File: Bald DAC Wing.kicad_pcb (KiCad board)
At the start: 4 copper layers, 45.5 x 46.5 mm, 50 parts, among them J1 PWR, J2 DAC_A_Out, J3 DAC_B_Out, J5 Z_Out, J6 Feather, J7 Data Debug Low, J8 High, U1 AD5447, U2 AD8065ARTZ, U3 AD8065ARTZ, U4 74LVC574APWR, U5 74LVC574APWR, U6 74LVC1G04, U7 REF3425

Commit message: It's getting there
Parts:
- removed J8: High, Connector_PinHeader_2.54mm:PinHeader_2x06_P2.54mm_Vertical
- removed TP12, TP13: TestPoint_Harwin, My Libraries:Harwin-S1751-46-Test-Point
- added H2: MountingHole_M2.5_Screw, MountingHole:MountingHole_2.7mm_M2.5, F.Cu at (102.5, 71.0)
- added J10: Ctrl Debug, Connector_PinHeader_2.54mm:PinHeader_2x04_P2.54mm_Vertical, F.Cu at (113.5, 86.3)
- added J9: Data Debug High, Connector_PinHeader_2.54mm:PinHeader_2x04_P2.54mm_Vertical, F.Cu at (113.5, 74.2)
- J7: footprint Connector_PinHeader_2.54mm:PinHeader_2x06_P2.54mm_Vertical -> Connector_PinHeader_2.54mm:PinHeader_2x04_P2.54mm_Vertical
- moved R73 8.32 mm to (118.8, 92.0), turned to 90 degrees
- moved C5 6.79 mm to (125.6, 97.2), turned to -90 degrees
- moved D1 5.07 mm to (122.5, 70.5)
- moved R61 5.07 mm to (126.5, 70.5)
- moved J7 4.81 mm to (113.5, 98.5)
- moved C15 4.33 mm to (108.0, 87.8), turned to 0 degrees
- moved C1 3.88 mm to (127.0, 76.0)
- moved C6 3.88 mm to (121.0, 76.0)
- moved TP6 3.88 mm to (123.7, 72.5)
- moved U2 3.88 mm to (123.7, 76.0)
- moved C11 3.54 mm to (124.5, 111.5)
- moved C12 3.54 mm to (117.5, 111.5)
- moved TP11 3.54 mm to (127.0, 111.5)
- moved TP5 3.54 mm to (115.0, 111.5)
- moved U7 3.54 mm to (121.5, 111.5)
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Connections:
- J7 pad 1: /DB3 -> /DB5
- J7 pad 2: /DB1 -> /DB4
- J7 pad 3: /DB2 -> /DB3
- J7 pad 4: /DB0 -> /DB2
- J7 pad 5: GND -> /DB1
- J7 pad 6: GND -> /DB0
- J7 pad 7: /DB7 -> GND
- J7 pad 8: /DB5 -> GND
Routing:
- net /DAC_AB: track 0.00 -> 52.1 mm, vias 0 -> 3
- net /~{CS}: track 0.00 -> 41.6 mm, vias 0 -> 1
- net /LCLKL: track 0.00 -> 41.5 mm, vias 0 -> 2
- net /LOE: track 0.00 -> 27.6 mm
- net /DB11: track 0.00 -> 24.3 mm
- net /DB0: track 0.00 -> 22.6 mm
- net /DB10: track 0.00 -> 22.6 mm
- net /DB1: track 0.00 -> 20.9 mm
- net /DB9: track 0.00 -> 20.7 mm
- net /LCLKH: track 0.00 -> 20.6 mm, vias 0 -> 1
- net /DB2: track 0.00 -> 19.2 mm
- net /DB8: track 0.00 -> 19.0 mm
- net /DB3: track 0.00 -> 17.6 mm
- net /DB7: track 0.00 -> 17.1 mm
- net /DB4: track 0.00 -> 16.2 mm
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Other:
- board size 45.5 x 46.5 mm -> 42 x 46.5 mm
- board text removed: "Should make it so feather sits over... adjust holes to match"

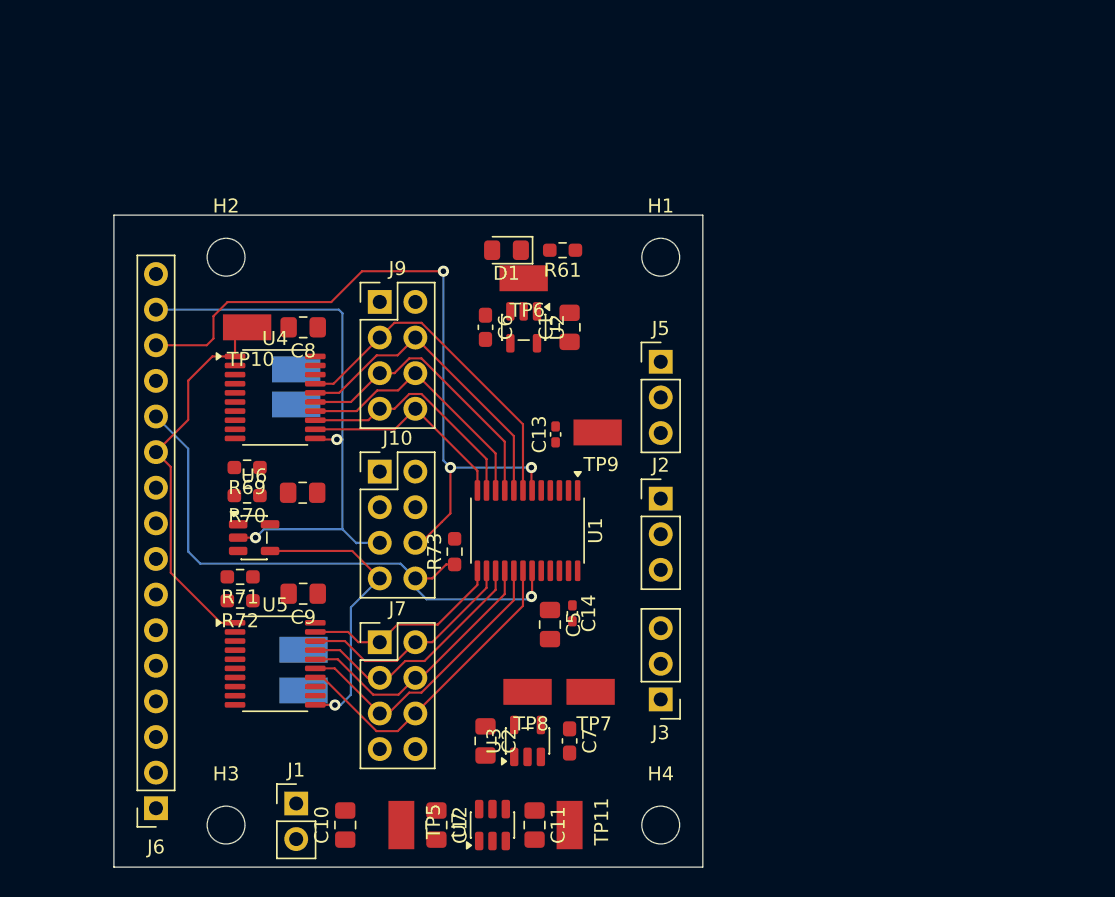
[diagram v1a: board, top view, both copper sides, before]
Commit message: added BNCs for ABZ
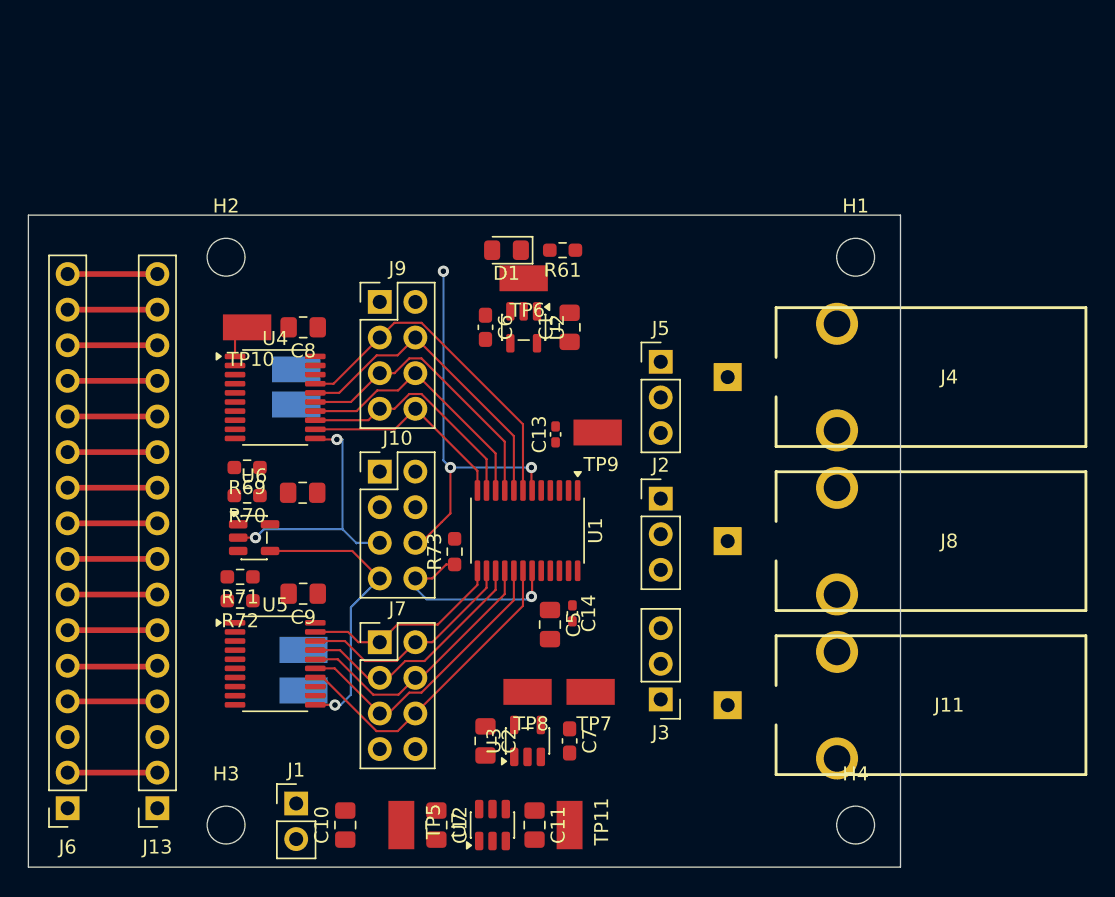
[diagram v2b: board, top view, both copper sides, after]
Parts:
- added J11: BNC_B, My Libraries:Molex_73100-0105_BNC_RA, F.Cu at (138.3, 103.0)
- added J13: Feather Debug, Connector_PinSocket_2.54mm:PinSocket_1x16_P2.54mm_Vertical, F.Cu at (97.6, 110.3)
- added J4: BNC_Z, My Libraries:Molex_73100-0105_BNC_RA, F.Cu at (138.3, 79.5)
- added J8: BNC_A, My Libraries:Molex_73100-0105_BNC_RA, F.Cu at (138.3, 91.2)
- moved H1 13.9 mm to (147.4, 71.0)
- moved H4 13.9 mm to (147.4, 111.5)
- moved J6 6.30 mm to (91.2, 110.3)
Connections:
- net Net-(J1-Pin_1) renamed /RawIn
- J5 pad 1: /Z_Blank -> unconnected-(J5-Pin_1-Pad1)
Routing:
- net /~{CS}: track 41.6 -> 20.5 mm
- net /LOE: track 27.6 -> 8.83 mm
- net /DAC_AB: track 52.1 -> 34.8 mm
- net /LCLKL: track 41.5 -> 25.5 mm
- net /D0: track 0.00 -> 6.45 mm
- net GND: track 0.00 -> 6.40 mm
- net /Z_Blank: track 0.00 -> 6.40 mm
- net /RawIn: track 0.00 -> 6.40 mm
- net /REF_EN: track 0.00 -> 6.40 mm
- net /D5: track 0.00 -> 6.40 mm
- net /D4: track 0.00 -> 6.40 mm
- net /D3: track 0.00 -> 6.40 mm
- net /D2: track 0.00 -> 6.40 mm
- net /D1: track 0.00 -> 6.40 mm
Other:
- board size 42 x 46.5 mm -> 62.2 x 46.5 mm

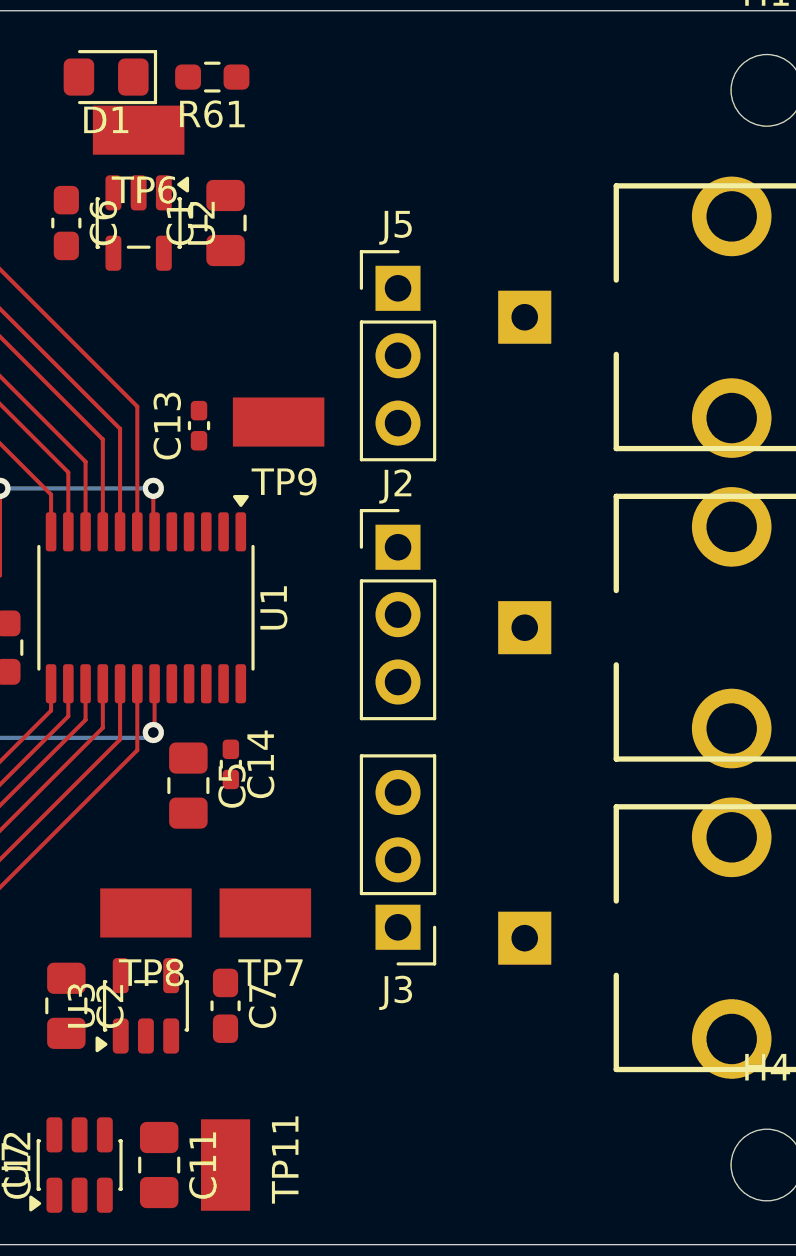
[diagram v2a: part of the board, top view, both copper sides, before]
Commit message: added JLC constraints (imported from clanker template)
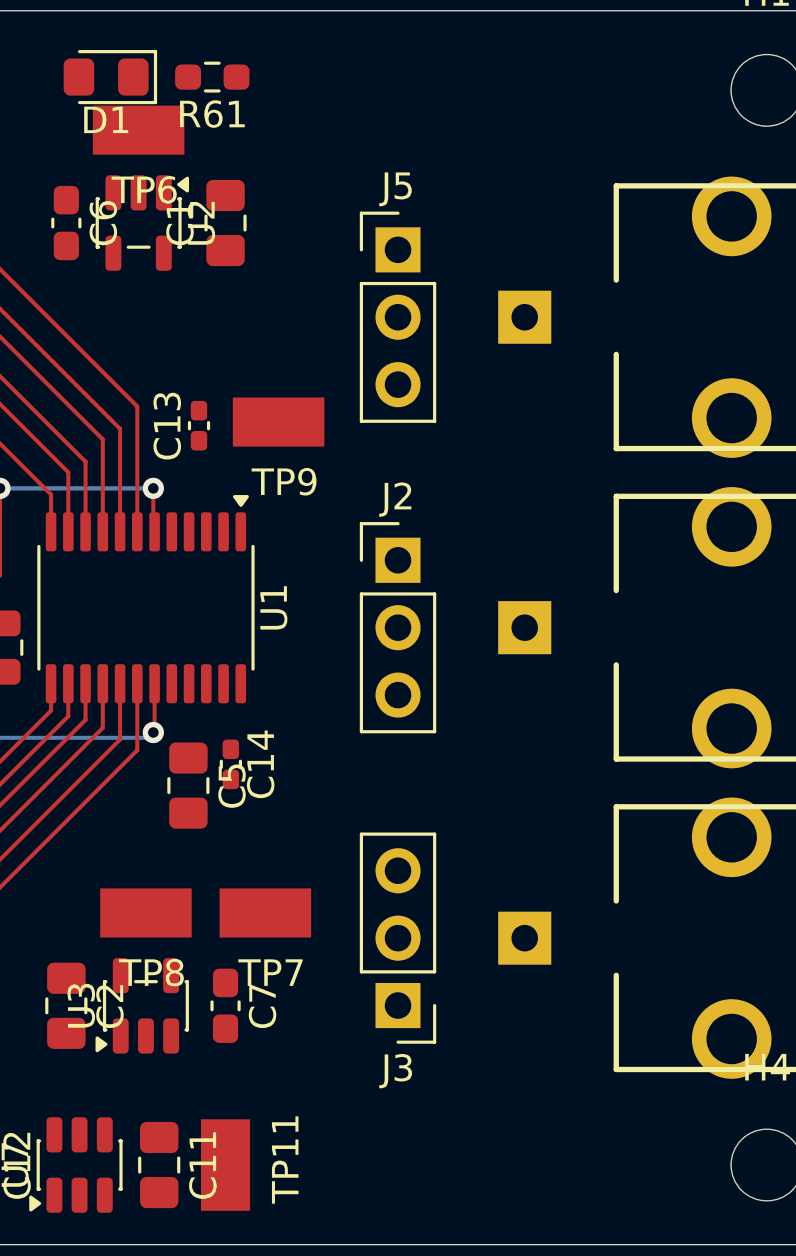
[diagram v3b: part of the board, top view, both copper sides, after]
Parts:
- moved J3 2.95 mm to (133.5, 105.5)
- moved J5 1.45 mm to (133.5, 77.0)
- moved J2 0.49 mm to (133.5, 88.7)
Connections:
- J2 pad 1: /OUT_A -> GND
- J2 pad 2: GND -> /OUT_A
- J3 pad 1: /OUT_B -> GND
- J3 pad 2: GND -> /OUT_B
- J5 pad 1: unconnected-(J5-Pin_1-Pad1) -> GND
- J5 pad 2: GND -> /Z_Blank
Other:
- rule pad_to_mask_clearance: 0.051 -> 0
- rule solder_mask_min_width: 0.1524 -> 0.1
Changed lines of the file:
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@@
 	(generator_version "10.0")
 	(general
-		(thickness 1.6)
+		(thickness 1.60596)
 		(legacy_teardrops no)
 	)
@@
 	(layers
 		(0 "F.Cu" signal)
-		(4 "In1.Cu" power "In1.Gnd.Cu")
-		(6 "In2.Cu" power "In2.3v3.Cu")
+		(4 "In1.Cu" signal)
+		(6 "In2.Cu" signal)
 		(2 "B.Cu" signal)
 		(9 "F.Adhes" user "F.Adhesive")
@@
 		(35 "F.Fab" user)
 		(33 "B.Fab" user)
+		(39 "User.1" user)
+		(41 "User.2" user)
+		(43 "User.3" user)
+		(45 "User.4" user)
 	)
 	(setup
@@
 			(layer "F.SilkS"
 				(type "Top Silk Screen")
-				(color "White")
 			)
 			(layer "F.Paste"
@@
 			(layer "F.Mask"
 				(type "Top Solder Mask")
-				(color "Red")
-				(thickness 0.01)
+				(thickness 0.01524)
+				(material "JLCPCB LPI soldermask")
+				(epsilon_r 3.8)
+				(loss_tangent 0)
 			)
 			(layer "F.Cu"
 				(type "copper")
-				(thickness 0.035)
+				(thickness 0.04064)
 			)
 			(layer "dielectric 1"
-				(type "core")
-				(thickness 0.48)
-				(material "FR4")
-				(epsilon_r 4.5)
+				(type "prepreg")
+				(thickness 0.0994)
+				(material "Nan Ya NP-155F 3313")
+				(epsilon_r 4.1)
 				(loss_tangent 0.02)
 			)
 			(layer "In1.Cu"
 				(type "copper")
-				(thickness 0.035)
+				(thickness 0.0152)
 			)
 			(layer "dielectric 2"
-				(type "prepreg")
-				(thickness 0.48)
-				(material "FR4")
-				(epsilon_r 4.5)
+				(type "core")
+				(thickness 1.265)
+				(material "Nan Ya NP-155F core")
+				(epsilon_r 4.43)
 				(loss_tangent 0.02)
 			)
 			(layer "In2.Cu"
 				(type "copper")
-				(thickness 0.035)
+				(thickness 0.0152)
 			)
 			(layer "dielectric 3"
-				(type "core")
-				(thickness 0.48)
-				(material "FR4")
-				(epsilon_r 4.5)
+				(type "prepreg")
+				(thickness 0.0994)
+				(material "Nan Ya NP-155F 3313")
+				(epsilon_r 4.1)
 				(loss_tangent 0.02)
 			)
 			(layer "B.Cu"
 				(type "copper")
-				(thickness 0.035)
+				(thickness 0.04064)
 			)
 			(layer "B.Mask"
 				(type "Bottom Solder Mask")
-				(color "Red")
-				(thickness 0.01)
+				(thickness 0.01524)
+				(material "JLCPCB LPI soldermask")
+				(epsilon_r 3.8)
+				(loss_tangent 0)
 			)
 			(layer "B.Paste"
@@
 			(layer "B.SilkS"
 				(type "Bottom Silk Screen")
-				(color "White")
 			)
 			(copper_finish "None")
-			(dielectric_constraints no)
+			(dielectric_constraints yes)
 		)
-		(pad_to_mask_clearance 0.051)
-		(solder_mask_min_width 0.1524)
+		(pad_to_mask_clearance 0)
+		(solder_mask_min_width 0.1)
 		(allow_soldermask_bridges_in_footprints no)
 		(tenting
@@
 		(capping no)
 		(filling no)
+		(zone_defaults)
 		(pcbplotparams
 			(layerselection 0x00000000_00000000_55555555_5755f5ff)
@@
 	(footprint "Connector_PinHeader_2.54mm:PinHeader_1x03_P2.54mm_Vertical"
 		(layer "F.Cu")
-		(at 133.5 88.2175)
+		(at 133.5 88.71)
 		(descr "Through hole straight pin header, 1x03, 2.54mm pitch, single row")
 		(tags "Through hole pin header THT 1x03 2.54mm single row")
@@
 			(layers "*.Cu" "*.Mask")
 			(remove_unused_layers no)
-			(net "/OUT_A")
+			(net "GND")
 			(pinfunction "Pin_1_1")
 			(pintype "passive")
@@
 			(layers "*.Cu" "*.Mask")
 			(remove_unused_layers no)
-			(net "GND")
+			(net "/OUT_A")
 			(pinfunction "Pin_2_2")
 			(pintype "passive")
@@
 	(footprint "Connector_PinHeader_2.54mm:PinHeader_1x03_P2.54mm_Vertical"
 		(layer "F.Cu")
-		(at 133.5 102.54 180)
+		(at 133.5 105.49 180)
 		(descr "Through hole straight pin header, 1x03, 2.54mm pitch, single row")
 		(tags "Through hole pin header THT 1x03 2.54mm single row")
@@
 			(layers "*.Cu" "*.Mask")
 			(remove_unused_layers no)
-			(net "/OUT_B")
+			(net "GND")
 			(pinfunction "Pin_1_1")
 			(pintype "passive")
@@
 			(layers "*.Cu" "*.Mask")
 			(remove_unused_layers no)
-			(net "GND")
+			(net "/OUT_B")
 			(pinfunction "Pin_2_2")
 			(pintype "passive")
@@
 	(footprint "Connector_PinHeader_2.54mm:PinHeader_1x03_P2.54mm_Vertical"
 		(layer "F.Cu")
-		(at 133.5 78.46)
+		(at 133.5 77.01)
 		(descr "Through hole straight pin header, 1x03, 2.54mm pitch, single row")
 		(tags "Through hole pin header THT 1x03 2.54mm single row")
@@
 			(layers "*.Cu" "*.Mask")
 			(remove_unused_layers no)
-			(net "unconnected-(J5-Pin_1-Pad1)")
+			(net "GND")
 			(pinfunction "Pin_1_1")
 			(pintype "passive")
@@
 			(layers "*.Cu" "*.Mask")
 			(remove_unused_layers no)
-			(net "GND")
+			(net "/Z_Blank")
 			(pinfunction "Pin_2_2")
 			(pintype "passive")

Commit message: data buses are done. see optimizations, but going to finish
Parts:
- removed R70, R71: 10k, Resistor_SMD:R_0603_1608Metric_Pad0.98x0.95mm_HandSolder
- removed TP1, TP2, TP3, TP4: TestPoint_Harwin, My Libraries:Harwin-S1751-46-Test-Point
- moved R72 9.10 mm to (103.6, 104.6), turned to 0 degrees
- moved U6 2.11 mm to (106.5, 91.6)
- moved R69 0.57 mm to (103.6, 85.6), turned to 0 degrees
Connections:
- R69 pad 2: Net-(U4-D1) -> Net-(U4-D0)
- R72 pad 2: Net-(U5-D7) -> Net-(U5-D6)
- U4 pad 18: Net-(U4-Q1) -> unconnected-(U4-Q1-Pad18)
- U4 pad 19: Net-(U4-Q0) -> unconnected-(U4-Q0-Pad19)
- U4 pad 3: Net-(U4-D1) -> Net-(U4-D0)
- U5 pad 12: Net-(U5-Q7) -> unconnected-(U5-Q7-Pad12)
- U5 pad 13: Net-(U5-Q6) -> unconnected-(U5-Q6-Pad13)
- U5 pad 9: Net-(U5-D7) -> Net-(U5-D6)
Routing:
- net /REF_EN: track 6.40 -> 75.3 mm
- net /Z_Blank: track 6.40 -> 58.9 mm
- net /D0: track 6.45 -> 32.3 mm, vias 0 -> 1
- net /D5: track 6.40 -> 31.4 mm, vias 0 -> 1
- net /D4: track 6.40 -> 31.2 mm, vias 0 -> 1
- net /D1: track 6.40 -> 31.2 mm, vias 0 -> 1
- net /D3: track 6.40 -> 31.1 mm, vias 0 -> 1
- net /D2: track 6.40 -> 31.0 mm, vias 0 -> 1
- net /LCLKL: track 25.5 -> 46.7 mm, vias 2 -> 1
- net Net-(U5-D6): track 0.00 -> 5.62 mm
- net /OUT_B: track 0.00 -> 4.78 mm
- net /OUT_A: track 0.00 -> 4.78 mm
- net /DB11: track 24.3 -> 25.9 mm
- net /DB9: track 20.7 -> 22.2 mm
- net /DB10: track 22.6 -> 24.1 mm
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
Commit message: removed Test Points for output because BNC and header pins give plenty of probe points
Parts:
- removed TP7, TP9: TestPoint_Harwin, My Libraries:Harwin-S1751-46-Test-Point

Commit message: doing power planes
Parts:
- moved D1 18.3 mm to (140.8, 71.2), turned to 0 degrees
- moved TP10 17.1 mm to (103.1, 93.1), turned to 90 degrees
- moved TP6 16.1 mm to (133.5, 85.3)
- moved J4 11.7 mm to (138.3, 91.2)
- moved J8 11.7 mm to (138.3, 79.5)
- moved J2 11.7 mm to (133.5, 77.0)
- moved J5 11.7 mm to (133.5, 88.7)
- moved C6 11.6 mm to (127.4, 85.7), turned to 0 degrees
- moved R61 10.3 mm to (136.8, 71.2), turned to 0 degrees
- moved R69 9.41 mm to (104.1, 76.2), turned to 180 degrees
- moved C2 8.33 mm to (129.3, 104.8), turned to 0 degrees
- moved TP8 8.13 mm to (129.9, 96.4), turned to -90 degrees
- moved U2 7.55 mm to (127.4, 82.6), turned to 90 degrees
- moved C1 6.72 mm to (124.4, 82.2), turned to -90 degrees
- moved C7 6.55 mm to (129.1, 99.3), turned to 180 degrees
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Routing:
- net /DAC_AB: track 34.8 -> 58.4 mm
- net /~{CS}: track 20.5 -> 43.6 mm
- net /LOE: track 8.83 -> 31.5 mm, vias 0 -> 1
- net /OUT_B: track 4.78 -> 21.3 mm
- net GND: track 6.40 -> 19.3 mm, vias 0 -> 11
- net Net-(U1-IOUTA): track 0.00 -> 12.6 mm
- net /Z_Blank: track 58.9 -> 69.2 mm, vias 0 -> 1
- net Net-(U1-IOUTB): track 0.00 -> 9.41 mm
- net +2V5: track 0.00 -> 9.34 mm, vias 0 -> 7
- net /OUT_A: track 4.78 -> 13.9 mm
- net /RawIn: track 6.40 -> 0.00 mm
- net +3V3: track 0.00 -> 6.27 mm, vias 0 -> 2
- net Net-(U4-D0): track 0.00 -> 4.67 mm
- net /REF_EN: track 75.3 -> 79.4 mm, vias 0 -> 1
- net /LCLKL: track 46.7 -> 48.3 mm
- added copper zone on F.Cu, net +2V5
- added copper zone on In2.Cu, net +2V5
- added copper zone on F.Cu, net +3V3
- added copper zone on In2.Cu, net +3V3
- added copper zone on F.Cu, net /RawIn
- added copper zone on F.Cu, net GND
- added copper zone on In1.Cu, net GND
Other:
- outline, holes or cut-outs redrawn
